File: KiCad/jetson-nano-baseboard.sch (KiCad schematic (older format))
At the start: 3 parts

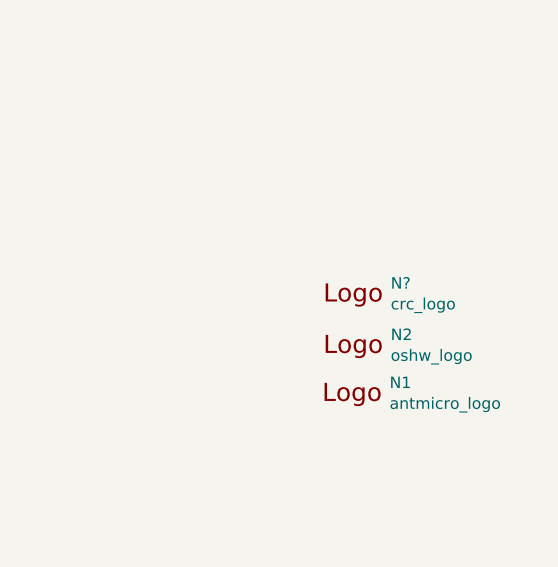
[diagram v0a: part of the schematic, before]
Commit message: Clean artefaccs, clean space for new DCDC
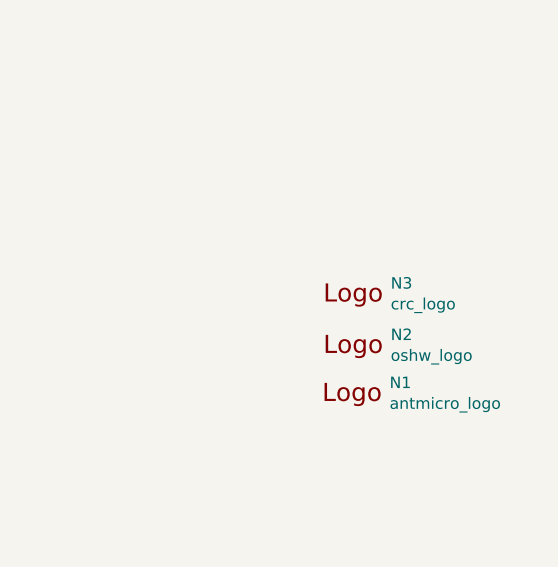
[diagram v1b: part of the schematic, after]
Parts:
- gave numbers to parts that had none: 1
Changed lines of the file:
@@
 $EndComp
 $Comp
-L jetson-nano-baseboard:crc_logo N?
+L jetson-nano-baseboard:crc_logo N3
 U 1 1 60CB08FE
 P 15125 9200
-F 0 "N?" H 15319 9203 50  0000 L CNN
+F 0 "N3" H 15319 9203 50  0000 L CNN
 F 1 "crc_logo" H 15319 9112 50  0000 L CNN
 F 2 "jetson-nano-baseboard-footprints:CRC_logo_15mm" H 15145 8960 50  0001 C CNN
